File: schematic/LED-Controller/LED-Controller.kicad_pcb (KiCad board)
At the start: 2 copper layers, 40 x 32 mm, 14 parts, among them J1 5V Power, J2 ICSP, J3 RCin, J4 Serial Connect, U1 PIC18F27Q43-xSO

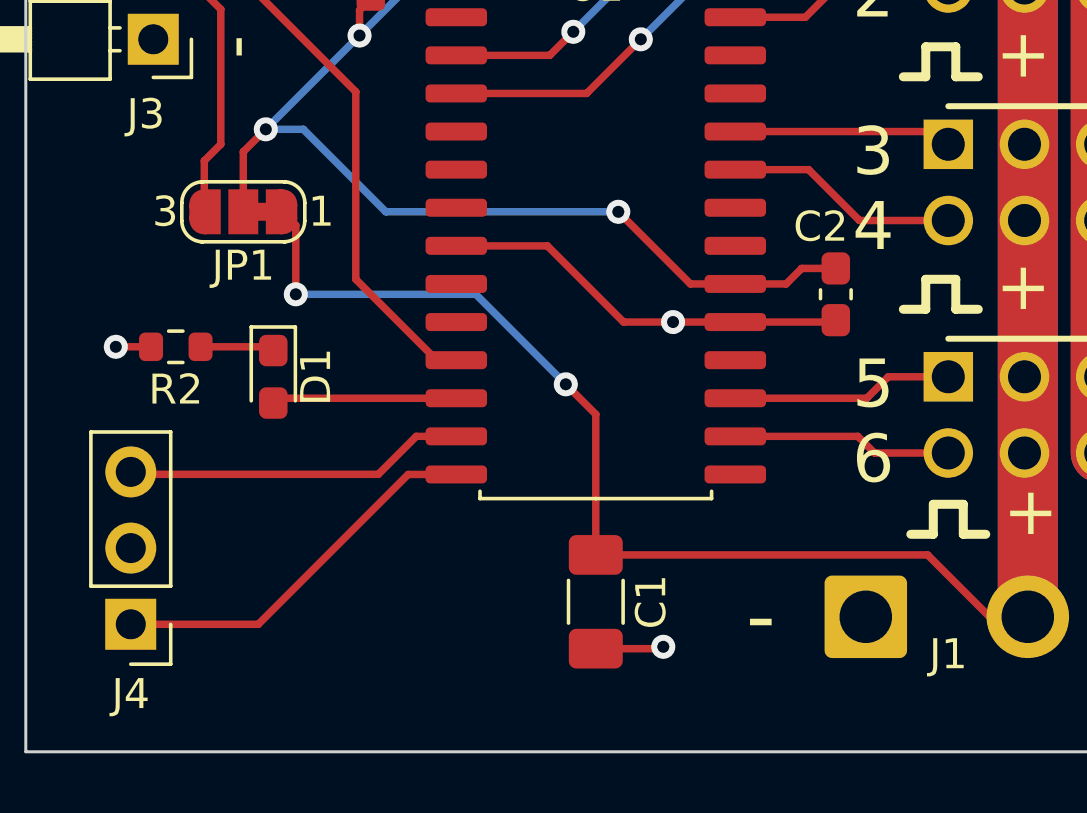
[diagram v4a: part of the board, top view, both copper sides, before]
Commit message: Converted to KiCad 6
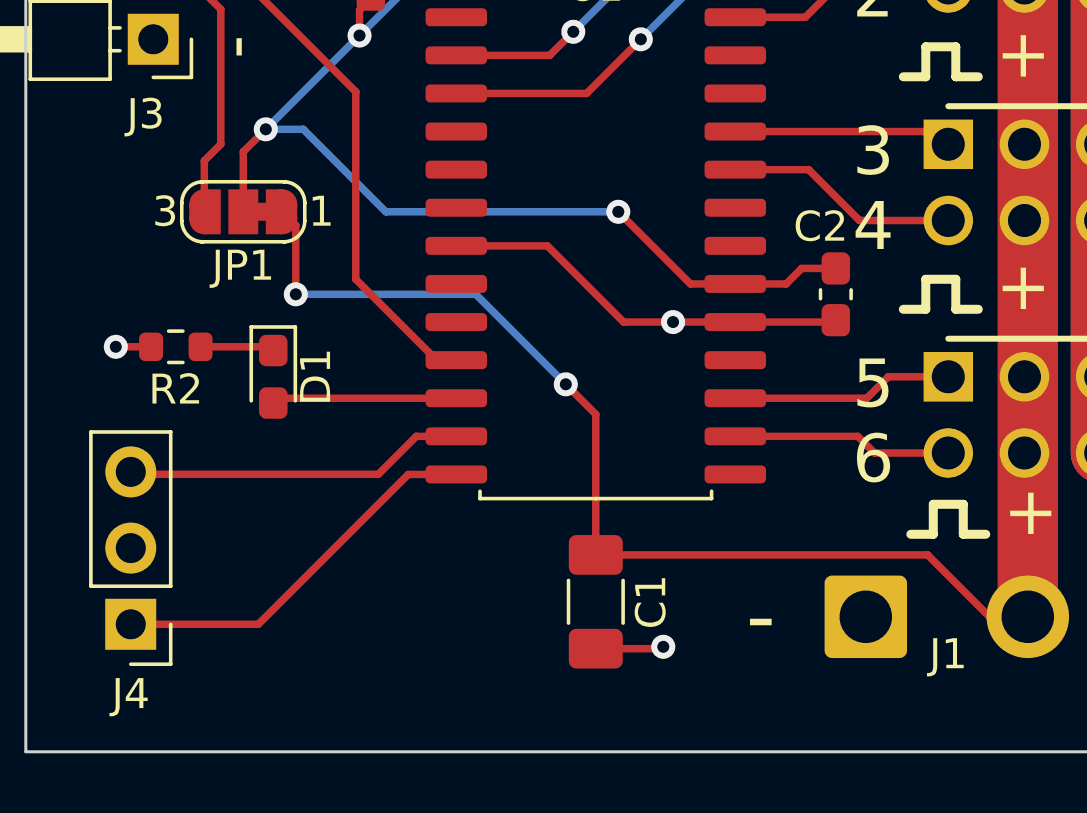
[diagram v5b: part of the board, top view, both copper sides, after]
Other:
- net class Default removed
